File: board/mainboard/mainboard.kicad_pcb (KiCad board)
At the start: 2 copper layers, 1.6 x 8.6 mm, 96 parts, among them P10 BUMPERS, P12 POWER, P4 SPI, P7 ANALOG, P8 OPTIONAL_PERIPH, SW1 SW_PUSH, SW2 SW_PUSH, SW3 SW_PUSH, SW4 SW_PUSH, U1 74LS138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

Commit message: Finished first draft of rev 1 board
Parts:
- removed BACKLIGHT: BACKL, PIN_ARRAY_2X1
- removed DAC: DAC, PIN_ARRAY_2X1
- removed P10: BUMPERS, PIN_ARRAY_2X1
- removed P12: POWER, PIN_ARRAY_2X1
- removed P4: SPI, 1x7_Headers
- added BUMPERS: BUMPERS, PIN_ARRAY_4x1, F.Cu at (175.3, 105.4)
- added J1: BACKL, PIN_ARRAY_2X1, F.Cu at (255.3, 154.9)
- added P5: DAC, PIN_ARRAY_2X1, F.Cu at (254.0, 105.4)
- added POT: 10K, P090_Potentiometer, F.Cu at (269.2, 121.9)
- added POWER: POWER, PIN_ARRAY_2X1, F.Cu at (273.1, 110.5)
- added SPI: SPI, 1x7_Headers, F.Cu at (204.5, 105.4)
- C16, C17: footprint CP8 -> CAP_8x6.2
- GLCD1: value GLCD -> NHD-C12832A1Z-NSW-BBW-3V3
- R10, R11, R13: moved to B.Cu
- moved U1 157.3 mm to (147.3, 128.3), turned to 90 degrees
- moved R1 155.1 mm to (132.1, 138.4), turned to 270 degrees
- moved X1 153.9 mm to (134.6, 138.4)
- moved R5 152.7 mm to (163.8, 110.5), turned to 90 degrees
- moved C28 151.2 mm to (261.6, 109.2), turned to 270 degrees
- moved C3 148.2 mm to (158.8, 135.9)
- moved R2 148.2 mm to (146.1, 144.8), turned to 90 degrees
- moved U3 139.2 mm to (135.9, 116.8), turned to 90 degrees
- moved R14 139.0 mm to (208.3, 109.2), turned to 180 degrees
- moved R3 138.7 mm to (171.4, 147.3), turned to 270 degrees
- moved C5 138.4 mm to (162.6, 135.9)
- moved MC2 138.3 mm to (163.8, 144.8), turned to 180 degrees
- moved R15 135.4 mm to (208.3, 111.8), turned to 180 degrees
- moved C2 135.1 mm to (156.2, 129.5), turned to 90 degrees
- moved C27 134.6 mm to (269.2, 110.5), turned to 90 degrees
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- renumbered P7 to ANALOG_IN
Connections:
- P8 pad 1: RTCINT1 -> MPUINT
- P8 pad 2: RTCINT2 -> WIFI_INT
- P8 pad 3: MPUINT -> RTCINT1
- P8 pad 4: SD_SWITCH -> RTCINT2
- P8 pad 5: MOTOR1F -> SD_SWITCH
- P8 pad 6: MOTOR2F -> MOTOR1F
- P8 pad 7: WIFI_INT -> MOTOR2F
- U1 pad 16: VCC -> 3V3
- U2 pad 14: VCC -> 3V3
- U3 pad 14: VCC -> 3V3
- U4 pad 14: VCC -> 3V3
- U5 pad 14: VCC -> 3V3
- WB1 pad 1: SPI_SCK_CC -> SPI_SCK
- WB1 pad 11: I2C_DA_CC -> I2C_DA
- WB1 pad 12: I2C_CL_CC -> I2C_CL
- WB1 pad 13: UART_RX_CC -> UART_RX
- WB1 pad 14: UART_TX_CC -> UART_TX
- WB1 pad 2: SPI_MOSI_CC -> SPI_MOSI
- WB1 pad 3: SPI_MISO_CC -> SPI_MISO
- WB1 pad 4: SPI_SEL0_CC -> SPI_SEL0
- WB1 pad 5: SPI_SEL1_CC -> SPI_SEL1
- WB1 pad 6: SPI_SEL2_CC -> SPI_SEL2
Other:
- board size 1.6 x 8.6 mm -> 148.6 x 58.4 mm
- net class Default: clearance 0.254 -> 0.1524; trace_width 0.254 -> 0.1524
- rule trace_clearance: 0.254 -> 0.1524
- rule trace_min: 0.254 -> 0.1524

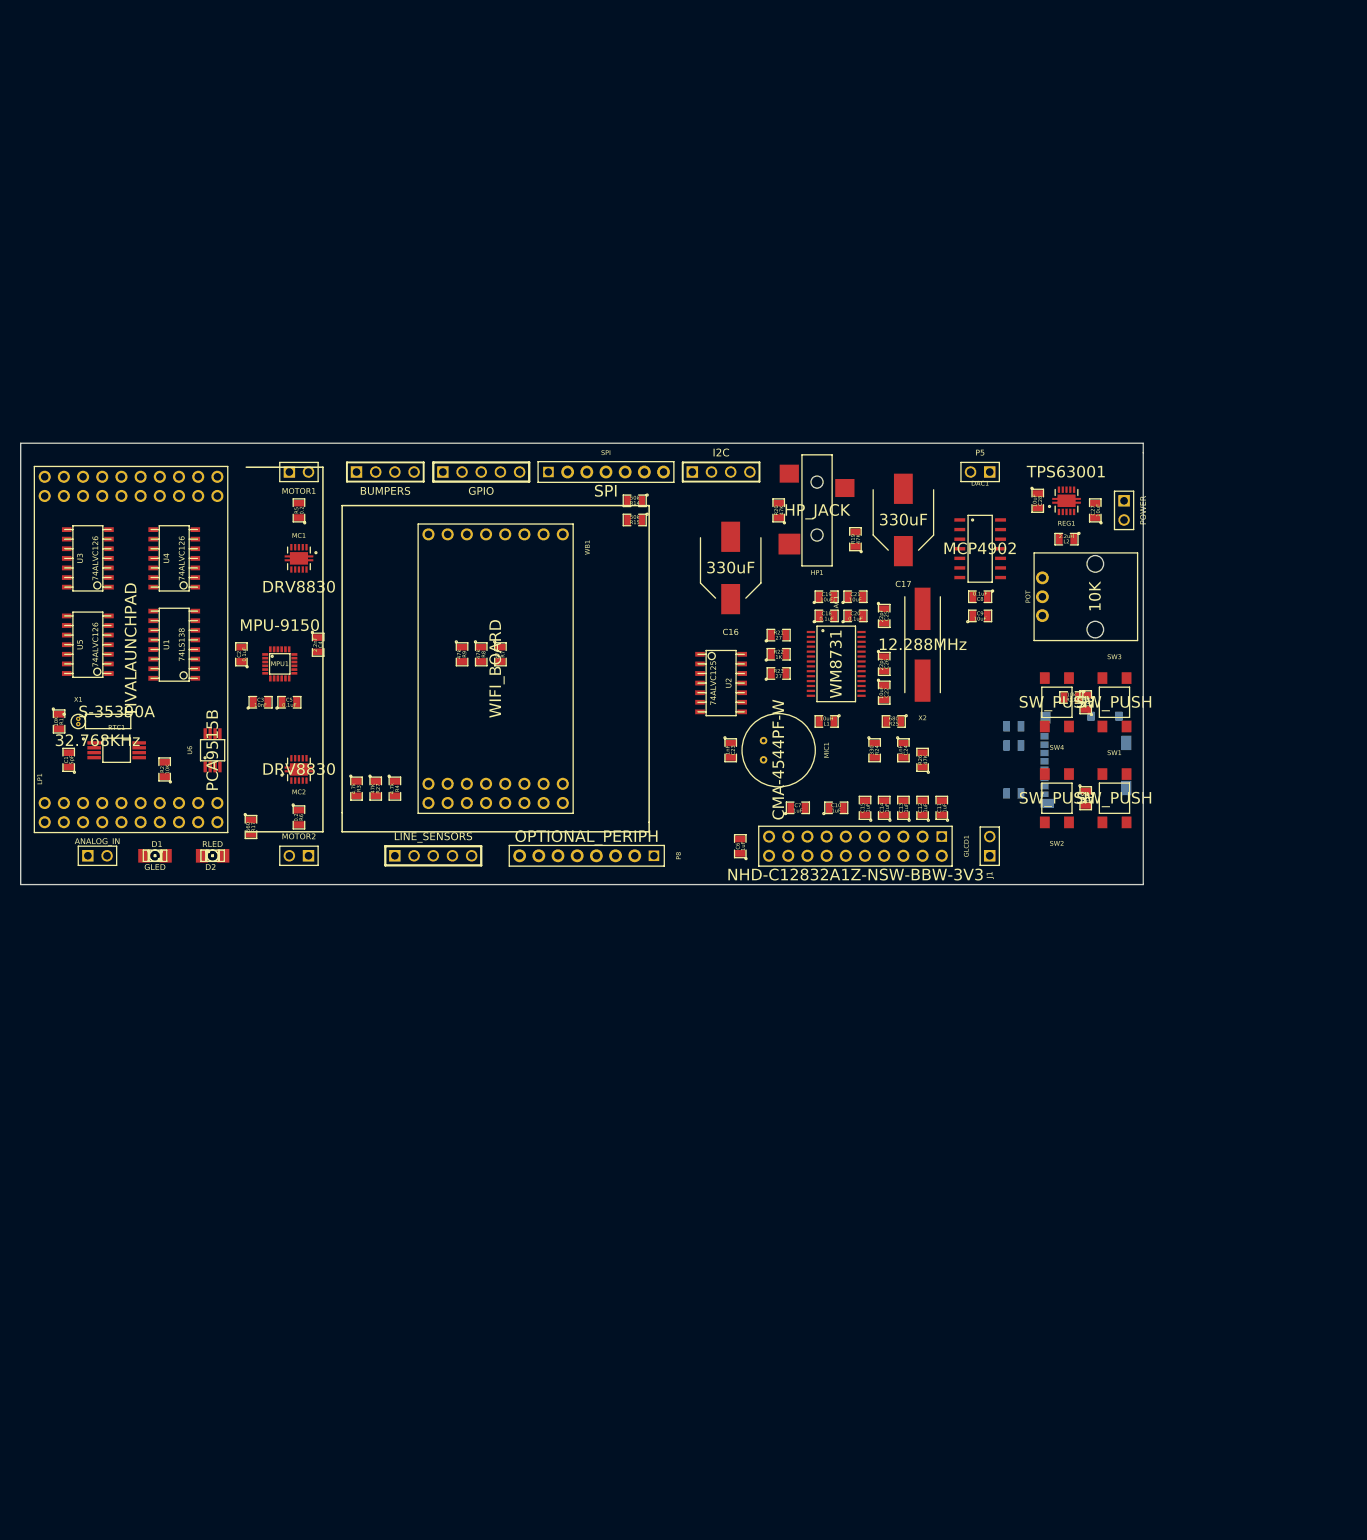
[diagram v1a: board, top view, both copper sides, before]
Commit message: Rev1.1 layout, without passives
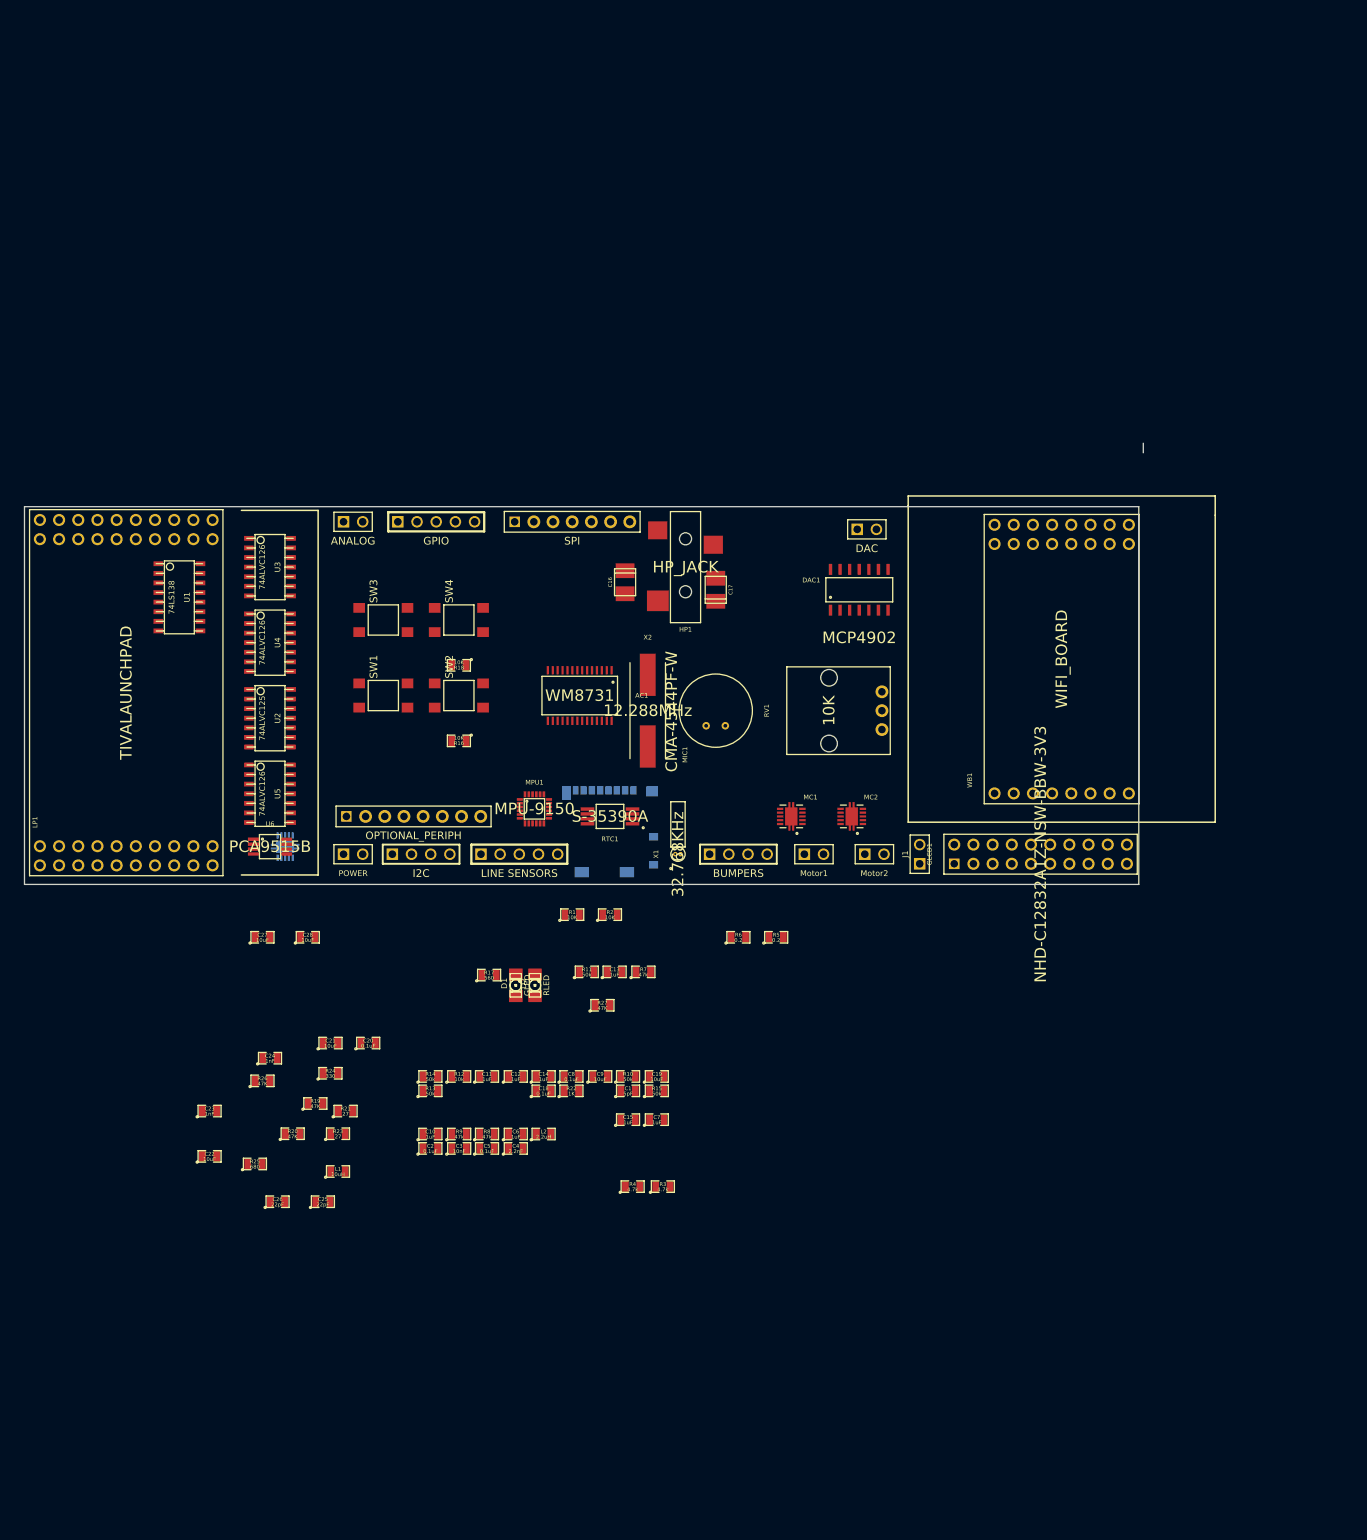
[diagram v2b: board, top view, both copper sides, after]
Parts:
- removed ANALOG_IN: ANALOG, PIN_ARRAY_2X1
- removed BUMPERS: BUMPERS, PIN_ARRAY_4x1
- removed GPIO: GPIO, PIN_ARRAY_5x1
- removed I2C: I2C, PIN_ARRAY_4x1
- removed LINE_SENSORS: CONN_5, PIN_ARRAY_5x1
- removed MOTOR1: Motor1, PIN_ARRAY_2X1
- removed MOTOR2: Motor2, PIN_ARRAY_2X1
- removed POT: 10K, P090_Potentiometer
- removed POWER: POWER, PIN_ARRAY_2X1
- removed SPI: SPI, 1x7_Headers
- added P1: I2C, PIN_ARRAY_4x1, F.Cu at (180.0, 156.0)
- added P10: BUMPERS, PIN_ARRAY_4x1, F.Cu at (222.0, 156.0)
- added P12: POWER, PIN_ARRAY_2X1, F.Cu at (171.0, 156.0)
- added P2: Motor1, PIN_ARRAY_2X1, F.Cu at (232.0, 156.0)
- added P3: Motor2, PIN_ARRAY_2X1, F.Cu at (240.0, 156.0)
- added P4: SPI, 1x7_Headers, F.Cu at (200.0, 112.0)
- added P6: LINE SENSORS, PIN_ARRAY_5x1, F.Cu at (193.0, 156.0)
- added P7: ANALOG, PIN_ARRAY_2X1, F.Cu at (171.0, 112.0)
- added P9: GPIO, PIN_ARRAY_5x1, F.Cu at (182.0, 112.0)
- added RV1: 10K, P090_Potentiometer, F.Cu at (234.0, 137.0)
- C16, C17: footprint CAP_8x6.2 -> c_tant_B
- R10, R11, R13: moved to F.Cu
- REG1: moved to B.Cu
- moved C27 123.9 mm to (159.0, 167.0), turned to 0 degrees
- moved REG1 113.1 mm to (162.0, 155.0)
- moved C28 112.6 mm to (165.0, 167.0), turned to 0 degrees
- moved C22 108.4 mm to (152.0, 196.0), turned to 0 degrees
- moved C25 107.4 mm to (167.0, 202.0), turned to 0 degrees
- moved C26 107.3 mm to (161.0, 202.0), turned to 0 degrees
- moved L2 104.8 mm to (196.2, 193.0), turned to 0 degrees
- moved R20 104.6 mm to (163.0, 193.0), turned to 0 degrees
- moved R19 103.4 mm to (166.0, 189.0), turned to 0 degrees
- moved R25 102.9 mm to (158.0, 197.0), turned to 0 degrees
- moved SW1 97.7 mm to (175.0, 135.0), turned to 90 degrees
- moved SW3 97.4 mm to (175.0, 125.0), turned to 90 degrees
- moved R26 97.2 mm to (159.0, 186.0), turned to 0 degrees
- moved R12 95.3 mm to (185.0, 185.4), turned to 0 degrees
- moved C24 93.2 mm to (160.0, 183.0), turned to 0 degrees
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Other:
- board size 148.6 x 58.4 mm -> 148.1 x 58.4 mm

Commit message: SPI and I2C busses nearly finished, Most traces in place, except for the longest ones
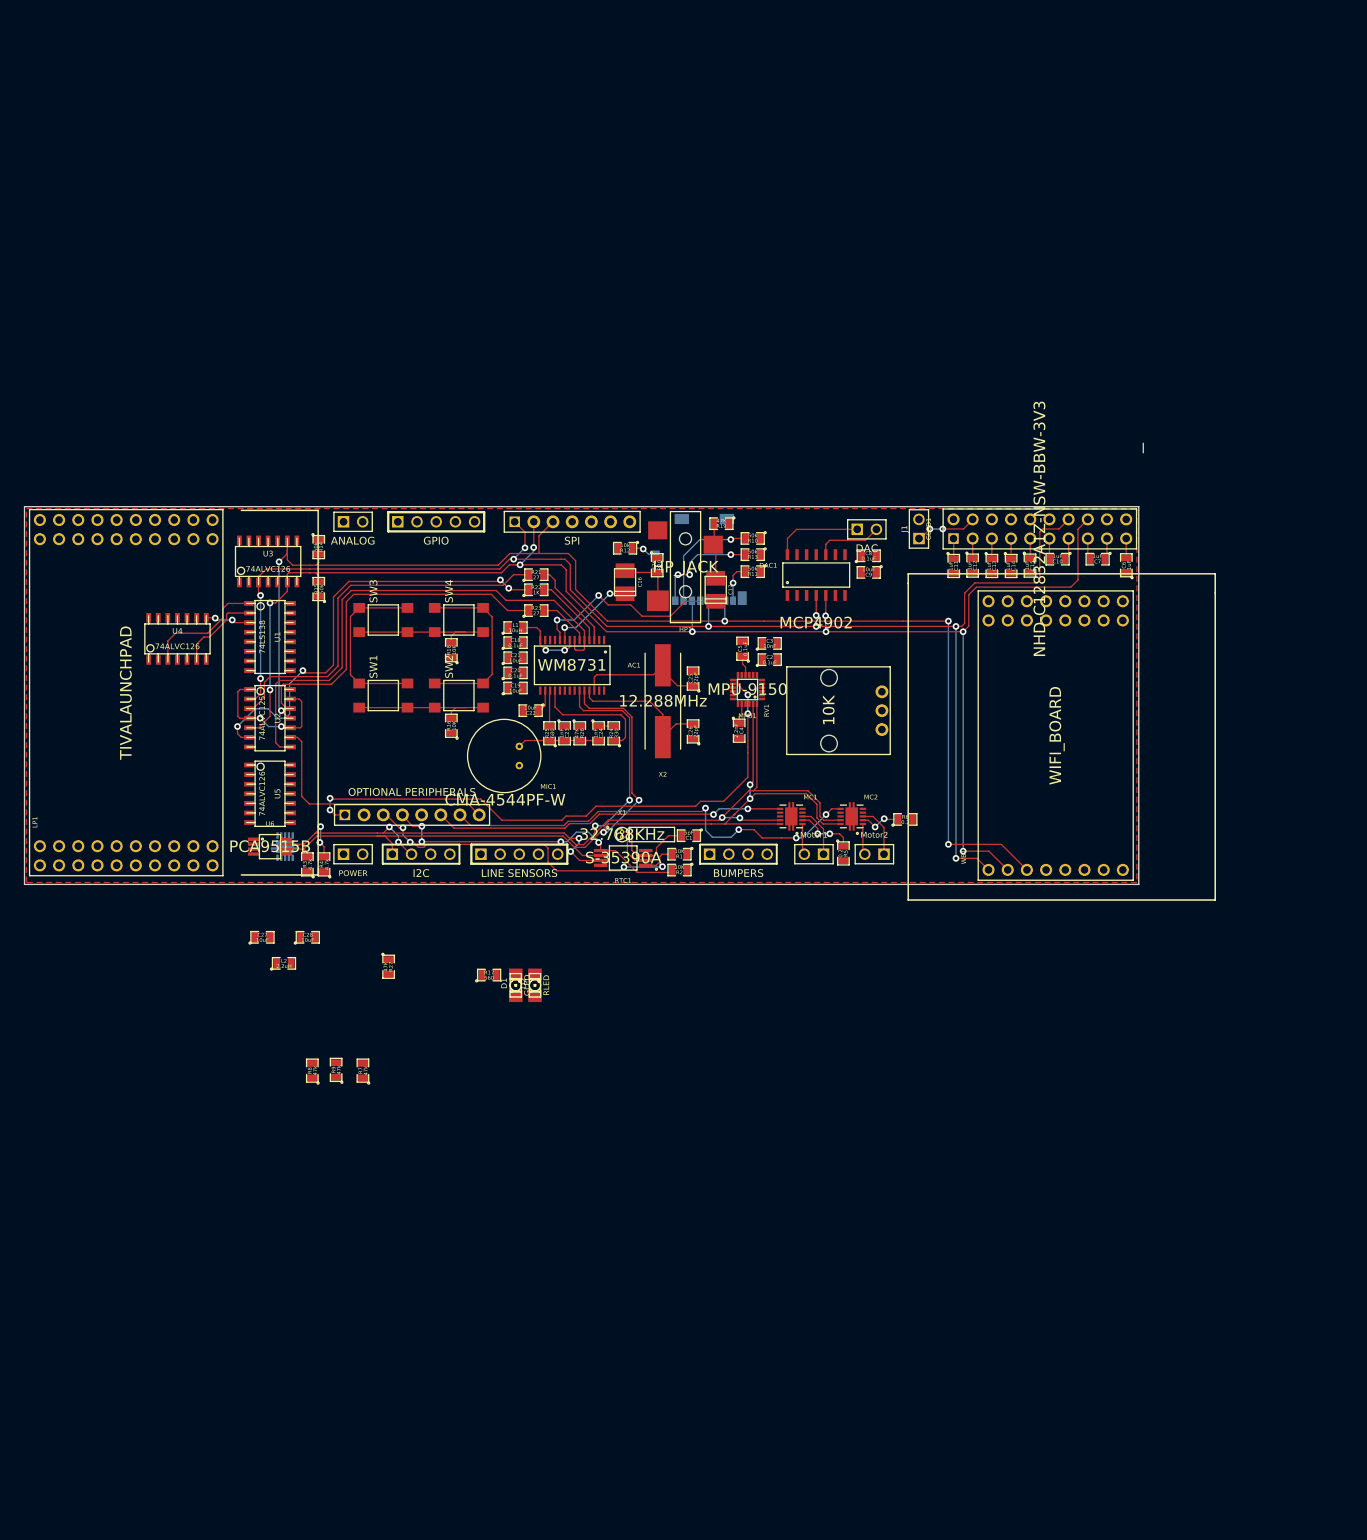
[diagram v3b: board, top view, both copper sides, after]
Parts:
- P8: value OPTIONAL_PERIPH -> OPTIONAL PERIPHERALS
- moved C10 112.6 mm to (264.2, 117.0), turned to 180 degrees
- moved C6 110.5 mm to (273.4, 117.8), turned to 90 degrees
- moved C7 94.4 mm to (269.6, 117.0), turned to 180 degrees
- moved R19 93.7 mm to (219.8, 112.2), turned to 180 degrees
- moved C14 91.6 mm to (258.1, 117.8), turned to 270 degrees
- moved C11 91.6 mm to (250.5, 117.8), turned to 270 degrees
- moved C12 90.7 mm to (253.0, 117.8), turned to 270 degrees
- moved C15 90.6 mm to (260.6, 117.8), turned to 270 degrees
- moved R20 89.4 mm to (211.2, 117.8), turned to 270 degrees
- moved C25 84.8 mm to (216.0, 132.8), turned to 90 degrees
- moved C26 83.1 mm to (216.0, 139.8), turned to 90 degrees
- moved R13 82.8 mm to (223.9, 116.3), turned to 180 degrees
- moved R15 80.1 mm to (166.4, 120.9), turned to 90 degrees
- moved C8 79.4 mm to (239.2, 116.5)
- moved C2 78.8 mm to (226.2, 130.2)
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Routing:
- net SPI_MOSI: track 0.00 -> 201.0 mm, vias 0 -> 9
- net SPI_SCK: track 0.00 -> 192.5 mm, vias 0 -> 9
- net SPI_MISO: track 0.00 -> 171.1 mm, vias 0 -> 5
- net I2C_DA: track 0.00 -> 146.5 mm, vias 0 -> 10
- net I2C_CL: track 0.00 -> 136.9 mm, vias 0 -> 4
- net MPUINT: track 0.00 -> 76.7 mm, vias 0 -> 4
- net N-00000109: track 0.00 -> 68.6 mm
- net N-00000100: track 0.00 -> 58.7 mm, vias 0 -> 4
- net MOTOR2F: track 0.00 -> 57.7 mm, vias 0 -> 4
- net N-0000097: track 0.00 -> 50.9 mm
- net N-00000110: track 0.00 -> 47.8 mm
- net RTCINT1: track 0.00 -> 47.6 mm, vias 0 -> 4
- net MOTOR1F: track 0.00 -> 46.7 mm, vias 0 -> 2
- net RTCINT2: track 0.00 -> 41.8 mm, vias 0 -> 4
- net AUD_DAC_CL: track 0.00 -> 33.4 mm
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- added copper zone on F.Cu, net GND
